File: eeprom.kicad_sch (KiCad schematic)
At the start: 1 part, among them U401 AT25DF041x-UxN-x

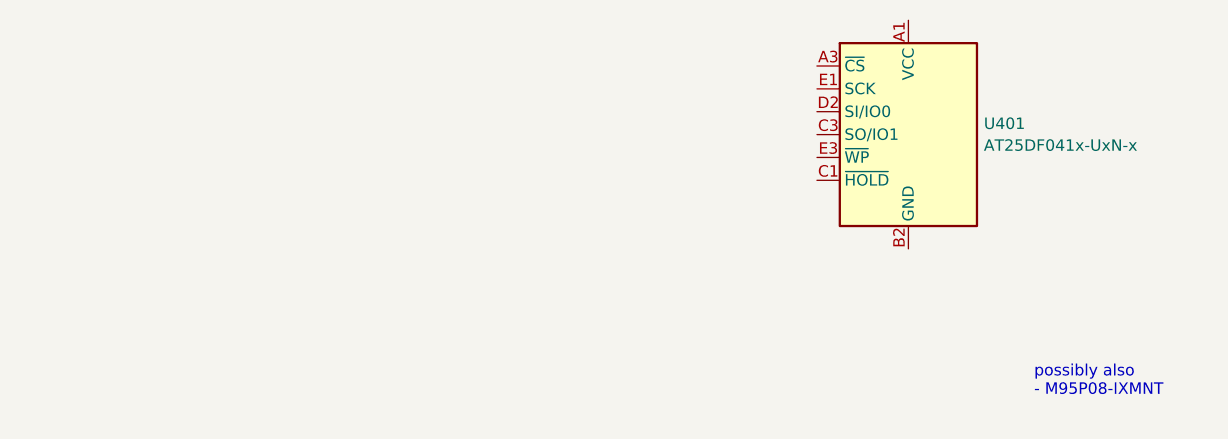
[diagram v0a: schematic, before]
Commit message: most of the components are placed
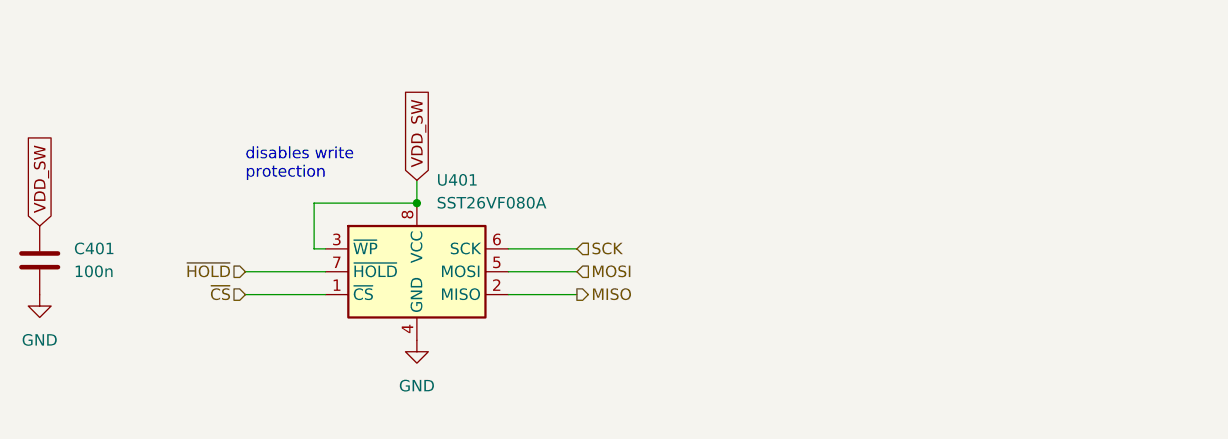
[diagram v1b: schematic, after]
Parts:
- removed U401: AT25DF041x-UxN-x, Package_CSP:WLCSP-8_1.58x1.63x0.35mm_Layout3x5_P0.35x0.4mm_Ball0.25mm_Pad0.25mm_NSMD, symbol Memory_Flash:AT25DF041x-UxN-x
- added C401: 100n, Capacitor_SMD:C_0402_1005Metric, symbol Device:C
- added U401: SST26VF080A, Package_DFN_QFN:WDFN-8-1EP_6x5mm_P1.27mm_EP3.4x4mm, symbol SST26VF080A:SST26VF080A
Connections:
- new net GND: C401.2, U401.4 (GND), U401.9 (GND)
- new net MISO: U401.2 (MISO)
- new net MOSI: U401.5 (MOSI)
- new net SCK: U401.6 (SCK)
- new net VDD_SW: C401.1, U401.3 (~{WP}), U401.8 (VCC)
- new net ~{CS}: U401.1 (~{CS})
- new net ~{HOLD}: U401.7 (~{HOLD})
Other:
- note added: "disables write protection"
- note removed: "possibly also - M95P08-IXMNT"
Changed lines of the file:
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@@
 (kicad_sch (version 20230121) (generator eeschema)
   (paper "A4")
-  (text "possibly also \n- M95P08-IXMNT" (at 199.39 109.22 0)
+  (junction (at 130.81 87.63) (diameter 0) (color 0 0 0 0)
+  )
+  (wire (pts (xy 119.38 87.63) (xy 119.38 92.71))
+    (stroke (width 0) (type default))
+  )
+  (wire (pts (xy 119.38 92.71) (xy 120.65 92.71))
+    (stroke (width 0) (type default))
+  )
+  (wire (pts (xy 140.97 92.71) (xy 148.59 92.71))
+    (stroke (width 0) (type default))
+  )
+  (wire (pts (xy 140.97 97.79) (xy 148.59 97.79))
+    (stroke (width 0) (type default))
+  )
+  (wire (pts (xy 111.76 97.79) (xy 120.65 97.79))
+    (stroke (width 0) (type default))
+  )
+  (wire (pts (xy 130.81 85.09) (xy 130.81 87.63))
+    (stroke (width 0) (type default))
+  )
+  (wire (pts (xy 140.97 95.25) (xy 148.59 95.25))
+    (stroke (width 0) (type default))
+  )
+  (wire (pts (xy 111.76 95.25) (xy 120.65 95.25))
+    (stroke (width 0) (type default))
+  )
+  (wire (pts (xy 130.81 87.63) (xy 119.38 87.63))
+    (stroke (width 0) (type default))
+  )
+  (text "disables write\nprotection" (at 111.76 85.09 0)
     (effects (font (size 1.27 1.27)) (justify left bottom))
   )
-  (symbol (lib_id "Memory_Flash:AT25DF041x-UxN-x") (at 185.42 80.01 0) (unit 1)
+  (global_label "VDD_SW" (shape input) (at 88.9 90.17 90) (fields_autoplaced)
+    (effects (font (size 1.27 1.27)) (justify left))
+    (property "Intersheetrefs" "${INTERSHEET_REFS}" (at 88.9 79.9277 90)
+      (effects (font (size 1.27 1.27)) (justify left) hide)
+    )
+  )
+  (global_label "VDD_SW" (shape input) (at 130.81 85.09 90) (fields_autoplaced)
+    (effects (font (size 1.27 1.27)) (justify left))
+    (property "Intersheetrefs" "${INTERSHEET_REFS}" (at 130.81 74.8477 90)
+      (effects (font (size 1.27 1.27)) (justify left) hide)
+    )
+  )
+  (hierarchical_label "SCK" (shape input) (at 148.59 92.71 0) (fields_autoplaced)
+    (effects (font (size 1.27 1.27)) (justify left))
+  )
+  (hierarchical_label "MOSI" (shape input) (at 148.59 95.25 0) (fields_autoplaced)
+    (effects (font (size 1.27 1.27)) (justify left))
+  )
+  (hierarchical_label "MISO" (shape output) (at 148.59 97.79 0) (fields_autoplaced)
+    (effects (font (size 1.27 1.27)) (justify left))
+  )
+  (hierarchical_label "~{HOLD}" (shape input) (at 111.76 95.25 180) (fields_autoplaced)
+    (effects (font (size 1.27 1.27)) (justify right))
+  )
+  (hierarchical_label "~{CS}" (shape input) (at 111.76 97.79 180) (fields_autoplaced)
+    (effects (font (size 1.27 1.27)) (justify right))
+  )
+  (symbol (lib_id "power:GND") (at 130.81 102.87 0) (unit 1)
     (in_bom yes) (on_board yes) (dnp no) (fields_autoplaced)
-    (property "Reference" "U401" (at 193.802 78.7979 0)
+    (property "Reference" "#PWR0402" (at 130.81 109.22 0)
+      (effects (font (size 1.27 1.27)) hide)
+    )
+    (property "Value" "GND" (at 130.81 107.95 0)
+      (effects (font (size 1.27 1.27)))
+    )
+    (property "Footprint" "" (at 130.81 102.87 0)
+      (effects (font (size 1.27 1.27)) hide)
+    )
+    (property "Datasheet" "" (at 130.81 102.87 0)
+      (effects (font (size 1.27 1.27)) hide)
+    )
+    (pin "1")
+    (instances
+      (project "lora-module"
+        (path "/30c7e509-35af-4828-996b-9681d057624f/466e04d9-bf2b-40f4-8878-cfff9e78e220"
+          (reference "#PWR0402") (unit 1)
+        )
+      )
+    )
+  )
+  (symbol (lib_id "power:GND") (at 88.9 97.79 0) (unit 1)
+    (in_bom yes) (on_board yes) (dnp no) (fields_autoplaced)
+    (property "Reference" "#PWR0401" (at 88.9 104.14 0)
+      (effects (font (size 1.27 1.27)) hide)
+    )
+    (property "Value" "GND" (at 88.9 102.87 0)
+      (effects (font (size 1.27 1.27)))
+    )
+    (property "Footprint" "" (at 88.9 97.79 0)
+      (effects (font (size 1.27 1.27)) hide)
+    )
+    (property "Datasheet" "" (at 88.9 97.79 0)
+      (effects (font (size 1.27 1.27)) hide)
+    )
+    (pin "1")
+    (instances
+      (project "lora-module"
+        (path "/30c7e509-35af-4828-996b-9681d057624f/466e04d9-bf2b-40f4-8878-cfff9e78e220"
+          (reference "#PWR0401") (unit 1)
+        )
+      )
+    )
+  )
+  (symbol (lib_id "SST26VF080A:SST26VF080A") (at 130.81 95.25 0) (unit 1)
+    (in_bom yes) (on_board yes) (dnp no) (fields_autoplaced)
+    (property "Reference" "U401" (at 133.0041 85.09 0)
       (effects (font (size 1.27 1.27)) (justify left))
     )
-    (property "Value" "AT25DF041x-UxN-x" (at 193.802 81.2221 0)
+    (property "Value" "SST26VF080A" (at 133.0041 87.63 0)
       (effects (font (size 1.27 1.27)) (justify left))
     )
-    (property "Footprint" "Package_CSP:WLCSP-8_1.58x1.63x0.35mm_Layout3x5_P0.35x0.4mm_Ball0.25mm_Pad0.25mm_NSMD" (at 180.34 95.25 0)
+    (property "Footprint" "Package_DFN_QFN:WDFN-8-1EP_6x5mm_P1.27mm_EP3.4x4mm" (at 129.54 86.36 0)
       (effects (font (size 1.27 1.27)) hide)
     )
-    (property "Datasheet" "http://www.adestotech.com/wp-content/uploads/DS-AT25DF041B_040.pdf" (at 185.42 62.23 0)
+    (property "Datasheet" "https://www.tme.eu/Document/bd96ccd0a160cf4e320b9da15fa415fa/26VF080A-104IMF.pdf" (at 132.08 105.41 0)
       (effects (font (size 1.27 1.27)) hide)
     )
-    (pin "A1")
-    (pin "A3")
-    (pin "B2")
-    (pin "C1")
-    (pin "C3")
-    (pin "D2")
-    (pin "E1")
-    (pin "E3")
+    (pin "1")
+    (pin "2")
+    (pin "3")
+    (pin "4")
+    (pin "5")
+    (pin "6")
+    (pin "7")
+    (pin "8")
+    (pin "9")
     (instances
       (project "lora-module"
@@
         )
       )
+    )
+  )
+  (symbol (lib_id "Device:C") (at 88.9 93.98 0) (unit 1)
+    (in_bom yes) (on_board yes) (dnp no) (fields_autoplaced)
+    (property "Reference" "C401" (at 92.71 92.71 0)
+      (effects (font (size 1.27 1.27)) (justify left))
+    )
+    (property "Value" "100n" (at 92.71 95.25 0)
+      (effects (font (size 1.27 1.27)) (justify left))
+    )
+    (property "Footprint" "Capacitor_SMD:C_0402_1005Metric" (at 89.8652 97.79 0)
+      (effects (font (size 1.27 1.27)) hide)
+    )
+    (property "Datasheet" "~" (at 88.9 93.98 0)
+      (effects (font (size 1.27 1.27)) hide)
+    )
+    (pin "1")
+    (pin "2")
+    (instances
+      (project "lora-module"
+        (path "/30c7e509-35af-4828-996b-9681d057624f/466e04d9-bf2b-40f4-8878-cfff9e78e220"
+          (reference "C401") (unit 1)
+        )
+      )

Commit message: groundplane settings tweak
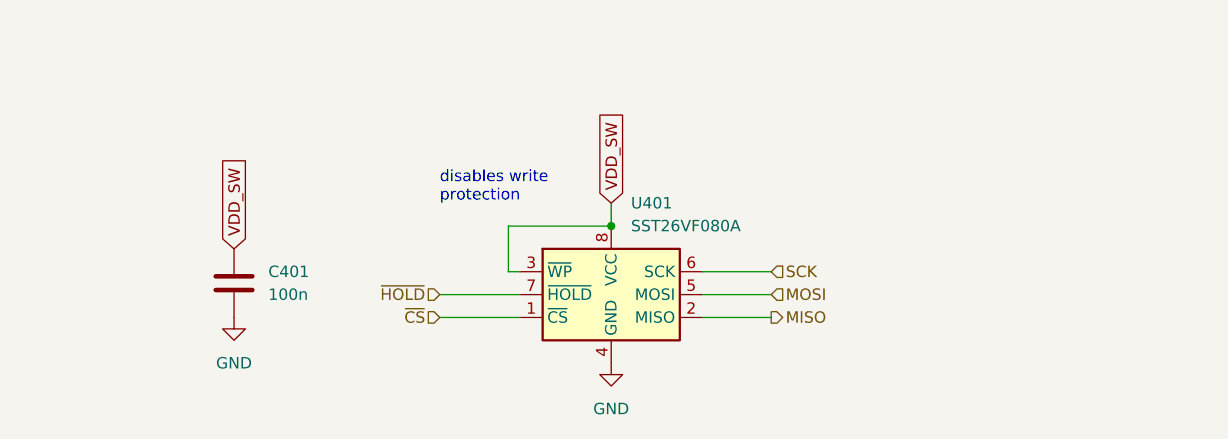
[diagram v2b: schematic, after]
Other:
- moved on the sheet: C401, U401
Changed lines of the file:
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@@
 (kicad_sch (version 20230121) (generator eeschema)
   (paper "A4")
-  (junction (at 130.81 87.63) (diameter 0) (color 0 0 0 0)
+  (junction (at 152.4 90.17) (diameter 0) (color 0 0 0 0)
   )
-  (wire (pts (xy 119.38 87.63) (xy 119.38 92.71))
+  (wire (pts (xy 140.97 90.17) (xy 140.97 95.25))
     (stroke (width 0) (type default))
   )
-  (wire (pts (xy 119.38 92.71) (xy 120.65 92.71))
+  (wire (pts (xy 140.97 95.25) (xy 142.24 95.25))
     (stroke (width 0) (type default))
   )
-  (wire (pts (xy 140.97 92.71) (xy 148.59 92.71))
+  (wire (pts (xy 162.56 95.25) (xy 170.18 95.25))
     (stroke (width 0) (type default))
   )
-  (wire (pts (xy 140.97 97.79) (xy 148.59 97.79))
+  (wire (pts (xy 162.56 100.33) (xy 170.18 100.33))
     (stroke (width 0) (type default))
   )
-  (wire (pts (xy 111.76 97.79) (xy 120.65 97.79))
+  (wire (pts (xy 133.35 100.33) (xy 142.24 100.33))
     (stroke (width 0) (type default))
   )
-  (wire (pts (xy 130.81 85.09) (xy 130.81 87.63))
+  (wire (pts (xy 152.4 87.63) (xy 152.4 90.17))
     (stroke (width 0) (type default))
   )
-  (wire (pts (xy 140.97 95.25) (xy 148.59 95.25))
+  (wire (pts (xy 162.56 97.79) (xy 170.18 97.79))
     (stroke (width 0) (type default))
   )
-  (wire (pts (xy 111.76 95.25) (xy 120.65 95.25))
+  (wire (pts (xy 133.35 97.79) (xy 142.24 97.79))
     (stroke (width 0) (type default))
   )
-  (wire (pts (xy 130.81 87.63) (xy 119.38 87.63))
+  (wire (pts (xy 152.4 90.17) (xy 140.97 90.17))
     (stroke (width 0) (type default))
   )
-  (text "disables write\nprotection" (at 111.76 85.09 0)
+  (text "disables write\nprotection" (at 133.35 87.63 0)
     (effects (font (size 1.27 1.27)) (justify left bottom))
   )
-  (global_label "VDD_SW" (shape input) (at 88.9 90.17 90) (fields_autoplaced)
+  (global_label "VDD_SW" (shape input) (at 110.49 92.71 90) (fields_autoplaced)
     (effects (font (size 1.27 1.27)) (justify left))
-    (property "Intersheetrefs" "${INTERSHEET_REFS}" (at 88.9 79.9277 90)
+    (property "Intersheetrefs" "${INTERSHEET_REFS}" (at 110.49 82.4677 90)
       (effects (font (size 1.27 1.27)) (justify left) hide)
     )
   )
-  (global_label "VDD_SW" (shape input) (at 130.81 85.09 90) (fields_autoplaced)
+  (global_label "VDD_SW" (shape input) (at 152.4 87.63 90) (fields_autoplaced)
     (effects (font (size 1.27 1.27)) (justify left))
-    (property "Intersheetrefs" "${INTERSHEET_REFS}" (at 130.81 74.8477 90)
+    (property "Intersheetrefs" "${INTERSHEET_REFS}" (at 152.4 77.3877 90)
       (effects (font (size 1.27 1.27)) (justify left) hide)
     )
   )
-  (hierarchical_label "SCK" (shape input) (at 148.59 92.71 0) (fields_autoplaced)
+  (hierarchical_label "SCK" (shape input) (at 170.18 95.25 0) (fields_autoplaced)
     (effects (font (size 1.27 1.27)) (justify left))
   )
-  (hierarchical_label "MOSI" (shape input) (at 148.59 95.25 0) (fields_autoplaced)
+  (hierarchical_label "MOSI" (shape input) (at 170.18 97.79 0) (fields_autoplaced)
     (effects (font (size 1.27 1.27)) (justify left))
   )
-  (hierarchical_label "MISO" (shape output) (at 148.59 97.79 0) (fields_autoplaced)
+  (hierarchical_label "MISO" (shape output) (at 170.18 100.33 0) (fields_autoplaced)
     (effects (font (size 1.27 1.27)) (justify left))
   )
-  (hierarchical_label "~{HOLD}" (shape input) (at 111.76 95.25 180) (fields_autoplaced)
+  (hierarchical_label "~{HOLD}" (shape input) (at 133.35 97.79 180) (fields_autoplaced)
     (effects (font (size 1.27 1.27)) (justify right))
   )
-  (hierarchical_label "~{CS}" (shape input) (at 111.76 97.79 180) (fields_autoplaced)
+  (hierarchical_label "~{CS}" (shape input) (at 133.35 100.33 180) (fields_autoplaced)
     (effects (font (size 1.27 1.27)) (justify right))
   )
-  (symbol (lib_id "power:GND") (at 130.81 102.87 0) (unit 1)
+  (symbol (lib_id "power:GND") (at 152.4 105.41 0) (unit 1)
     (in_bom yes) (on_board yes) (dnp no) (fields_autoplaced)
-    (property "Reference" "#PWR0402" (at 130.81 109.22 0)
+    (property "Reference" "#PWR0402" (at 152.4 111.76 0)
       (effects (font (size 1.27 1.27)) hide)
     )
-    (property "Value" "GND" (at 130.81 107.95 0)
+    (property "Value" "GND" (at 152.4 110.49 0)
       (effects (font (size 1.27 1.27)))
     )
-    (property "Footprint" "" (at 130.81 102.87 0)
+    (property "Footprint" "" (at 152.4 105.41 0)
       (effects (font (size 1.27 1.27)) hide)
     )
-    (property "Datasheet" "" (at 130.81 102.87 0)
+    (property "Datasheet" "" (at 152.4 105.41 0)
       (effects (font (size 1.27 1.27)) hide)
     )
@@
     )
   )
-  (symbol (lib_id "power:GND") (at 88.9 97.79 0) (unit 1)
+  (symbol (lib_id "power:GND") (at 110.49 100.33 0) (unit 1)
     (in_bom yes) (on_board yes) (dnp no) (fields_autoplaced)
-    (property "Reference" "#PWR0401" (at 88.9 104.14 0)
+    (property "Reference" "#PWR0401" (at 110.49 106.68 0)
       (effects (font (size 1.27 1.27)) hide)
     )
-    (property "Value" "GND" (at 88.9 102.87 0)
+    (property "Value" "GND" (at 110.49 105.41 0)
       (effects (font (size 1.27 1.27)))
     )
-    (property "Footprint" "" (at 88.9 97.79 0)
+    (property "Footprint" "" (at 110.49 100.33 0)
       (effects (font (size 1.27 1.27)) hide)
     )
-    (property "Datasheet" "" (at 88.9 97.79 0)
+    (property "Datasheet" "" (at 110.49 100.33 0)
       (effects (font (size 1.27 1.27)) hide)
     )
@@
     )
   )
-  (symbol (lib_id "SST26VF080A:SST26VF080A") (at 130.81 95.25 0) (unit 1)
+  (symbol (lib_id "SST26VF080A:SST26VF080A") (at 152.4 97.79 0) (unit 1)
     (in_bom yes) (on_board yes) (dnp no) (fields_autoplaced)
-    (property "Reference" "U401" (at 133.0041 85.09 0)
+    (property "Reference" "U401" (at 154.5941 87.63 0)
       (effects (font (size 1.27 1.27)) (justify left))
     )
-    (property "Value" "SST26VF080A" (at 133.0041 87.63 0)
+    (property "Value" "SST26VF080A" (at 154.5941 90.17 0)
       (effects (font (size 1.27 1.27)) (justify left))
     )
-    (property "Footprint" "Package_DFN_QFN:WDFN-8-1EP_6x5mm_P1.27mm_EP3.4x4mm" (at 129.54 86.36 0)
+    (property "Footprint" "Package_DFN_QFN:WDFN-8-1EP_6x5mm_P1.27mm_EP3.4x4mm" (at 151.13 88.9 0)
       (effects (font (size 1.27 1.27)) hide)
     )
-    (property "Datasheet" "https://www.tme.eu/Document/bd96ccd0a160cf4e320b9da15fa415fa/26VF080A-104IMF.pdf" (at 132.08 105.41 0)
+    (property "Datasheet" "https://www.tme.eu/Document/bd96ccd0a160cf4e320b9da15fa415fa/26VF080A-104IMF.pdf" (at 153.67 107.95 0)
       (effects (font (size 1.27 1.27)) hide)
     )
@@
     )
   )
-  (symbol (lib_id "Device:C") (at 88.9 93.98 0) (unit 1)
+  (symbol (lib_id "Device:C") (at 110.49 96.52 0) (unit 1)
     (in_bom yes) (on_board yes) (dnp no) (fields_autoplaced)
-    (property "Reference" "C401" (at 92.71 92.71 0)
+    (property "Reference" "C401" (at 114.3 95.25 0)
       (effects (font (size 1.27 1.27)) (justify left))
     )
-    (property "Value" "100n" (at 92.71 95.25 0)
+    (property "Value" "100n" (at 114.3 97.79 0)
       (effects (font (size 1.27 1.27)) (justify left))
     )
-    (property "Footprint" "Capacitor_SMD:C_0402_1005Metric" (at 89.8652 97.79 0)
+    (property "Footprint" "Capacitor_SMD:C_0402_1005Metric" (at 111.4552 100.33 0)
       (effects (font (size 1.27 1.27)) hide)
     )
-    (property "Datasheet" "~" (at 88.9 93.98 0)
+    (property "Datasheet" "~" (at 110.49 96.52 0)
       (effects (font (size 1.27 1.27)) hide)
     )
